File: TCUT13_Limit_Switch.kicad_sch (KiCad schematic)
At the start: 14 parts, among them J1 533980471, Q1 BC847, Q2 BC847, U1 TCUT1300X01

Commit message: [Sudhanshu] Endstop with final Setup
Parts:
- removed J1: 533980471, Molex_1.25_533980471:CON_533980471, symbol Molex_1.25_533980471_Pin_Veritcal:533980471
- added C1: 0.1uF_0603, morphle_footprints:Cap_0603_1608Metric, symbol morphle:0.1uF_0603
- added D2: LED_SMD_0603, morphle_footprints:LED_0603_1608Metric, symbol morphle_symbols:LED_SMD_0603
- added J1: 5055680471, morphle_footprints:MOLEX_5055680471, symbol Molex_1.25_5055680371:5055680471
- added R8: 1K_0603, morphle_footprints:R_0603_1608Metric, symbol morphle_symbols:1K_0603
- D1: footprint Diode_SMD:D_0402_1005Metric -> morphle_footprints:LED_0603_1608Metric
- R1, R2, R3, R4, R5, R6, R7: footprint Resistor_SMD:R_0402_1005Metric -> morphle_footprints:R_0603_1608Metric
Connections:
- net +3.3V: now also C1.1, J1.2
- net GND: now also C1.2, D2.1 (K), J1.1, J1.S1 (SHIELD1), J1.S2 (SHIELD2)
- net output1: now also J1.4
- net output2: now also J1.3, R8.1
- new net: D2.2 (A), R8.2

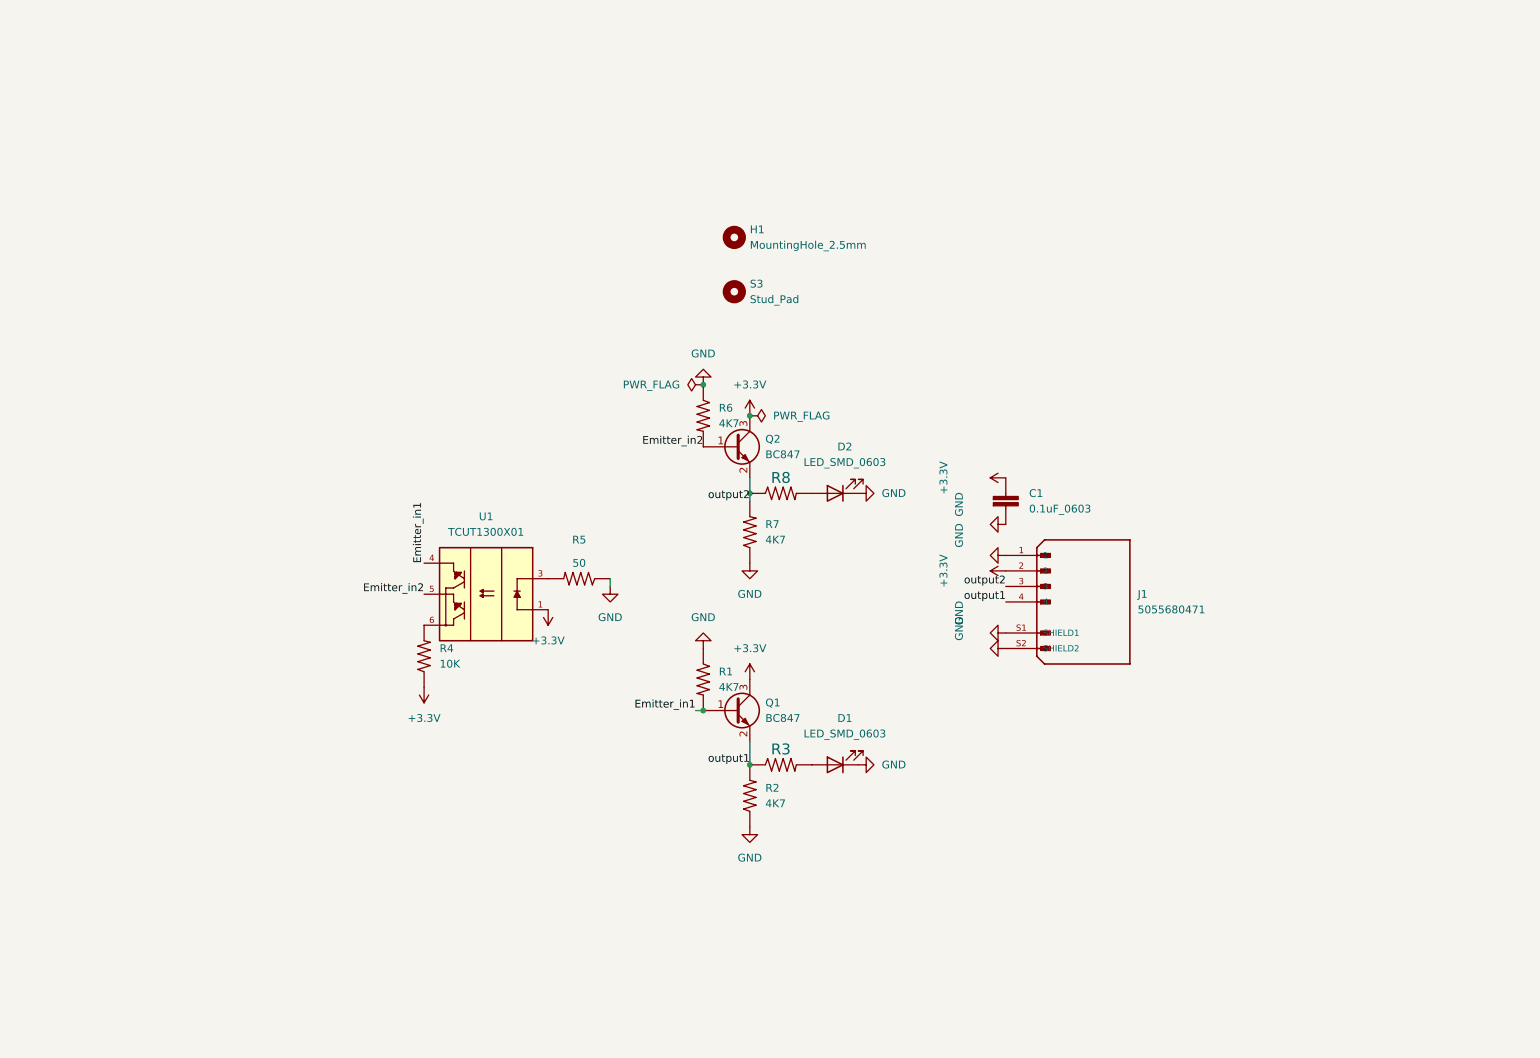
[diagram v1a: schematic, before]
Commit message: sudhanshu Final PCB with 2 Connector Right angle and upside Connector in a same place
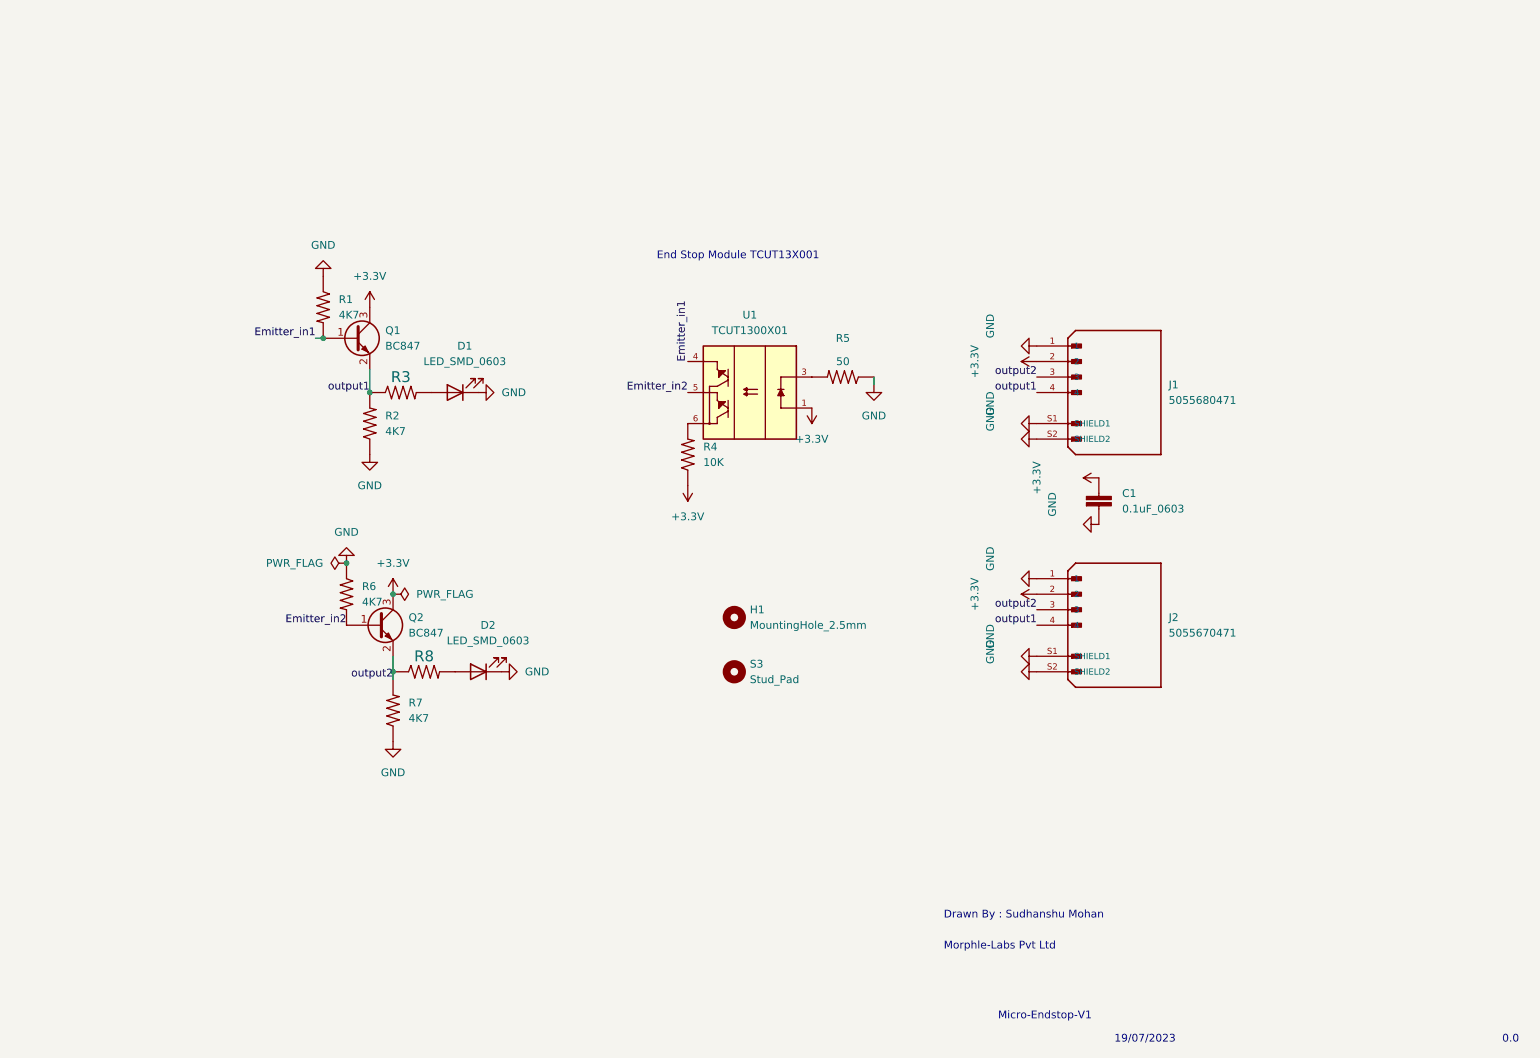
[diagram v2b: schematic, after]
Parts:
- added J2: 5055670471, molex_1.25_5055670471:MOLEX_5055670471, symbol Molex_1.25_5055670471:5055670471
- U1: footprint TCUT13XXX:XDCR_TCUT1300X01 -> TCUT13XX:XDCR_TCUT1300X01
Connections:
- net +3.3V: now also J2.2
- net GND: now also J2.1, J2.S1 (SHIELD1), J2.S2 (SHIELD2)
- net output1: now also J2.4
- net output2: now also J2.3
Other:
- note added: "0.0"
- note added: "19/07/2023"
- note added: "Drawn By : Sudhanshu Mohan"
- note added: "End Stop Module TCUT13X001"
- note added: "Micro-Endstop-V1"
- note added: "Morphle-Labs Pvt Ltd"
- moved on the sheet: C1, D1, D2, H1, J1, Q1, Q2, R1, R2, R3, R4, R5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

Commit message: Final PCB Edit
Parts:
- J1, J2: now not fitted; now left out of the parts list
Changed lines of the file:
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@@
   )
   (symbol (lib_id "Molex_1.25_5055680371:5055680471") (at 207.01 87.63 0) (unit 1)
-    (in_bom yes) (on_board yes) (dnp no) (fields_autoplaced)
+    (in_bom no) (on_board yes) (dnp yes) (fields_autoplaced)
     (property "Reference" "J1" (at 215.9 86.36 0)
       (effects (font (size 1.27 1.27)) (justify left))
@@
   )
   (symbol (lib_id "Molex_1.25_5055670471:5055670471") (at 207.01 125.73 0) (unit 1)
-    (in_bom yes) (on_board yes) (dnp no) (fields_autoplaced)
+    (in_bom no) (on_board yes) (dnp yes) (fields_autoplaced)
     (property "Reference" "J2" (at 215.9 124.46 0)
       (effects (font (size 1.27 1.27)) (justify left))

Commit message: [sudhasnhu] added Some Change New Repo
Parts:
- removed Q1, Q2: BC847, morphle_footprints:BC847, symbol morphle_symbols:BC847
- added U2, U3: BC857A, bc857:SOT95P240X110-3N, symbol BC857:BC857A
- H1: footprint MountingHole:MountingHole_2.5mm_Pad_Via -> MountingHole:MountingHole_2.7mm_M2.5_Pad_Via
- J1: now fitted
- R2: Resistance 4K7 -> 1k
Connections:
- net +3.3V: now also J1.4, J2.4, R2.2, R6.1, U2.2 (E), U3.2 (E); no longer J1.2, J2.2
- net Emitter_in1: now also R1.1; no longer R1.2
- net Emitter_in2: now also R7.1; no longer R6.2
- net GND: no longer R1.1, R2.1, R6.1, R7.1
- net output1: now also J1.2, J2.2, U2.3 (C); no longer J1.4, J2.4, R2.2
- net output2: now also U3.3 (C); no longer R7.2
- new net: R6.2, R7.2, U3.1 (B)
- new net: R1.2, R2.1, U2.1 (B)
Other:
- moved on the sheet: D1, D2, R1, R2, R3, R4, R5, R6, R7, R8, U1
